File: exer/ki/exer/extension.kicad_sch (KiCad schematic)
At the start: 17 parts, among them J1 Conn_01x20, J2 Conn_01x20, J3 Conn_01x34, J4 Conn_01x34, U10 74HCT574, U11 74HCT574, U12 74LS125, U13 74LS125, U14 74HCT574

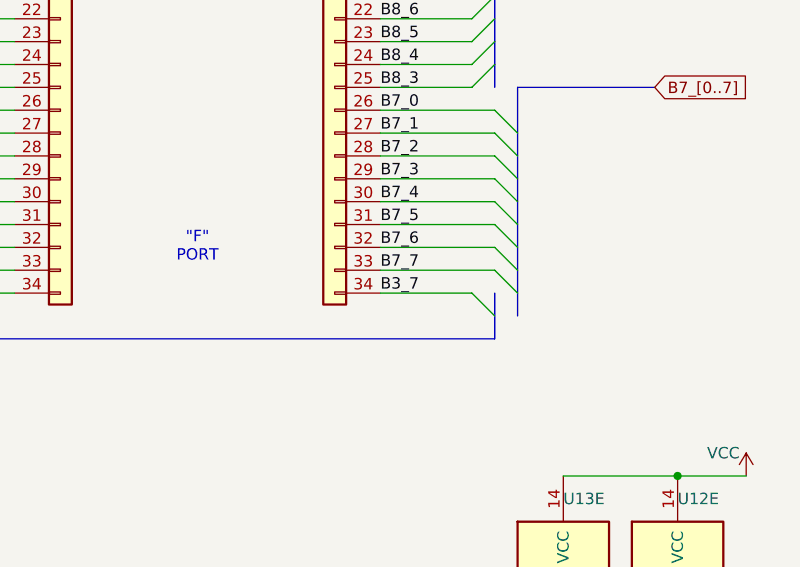
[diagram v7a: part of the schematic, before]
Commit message: Factor out functions for the t, s, and g commands to the Nano and fix a wiring error in KiCad.
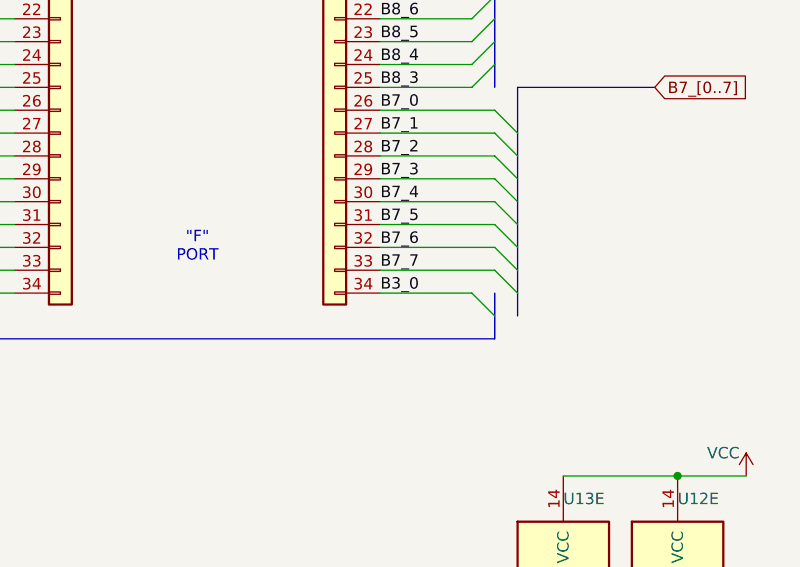
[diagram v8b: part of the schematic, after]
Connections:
- net B3_0: now also J4.34 (Pin_34)
- net B3_7: no longer J4.34 (Pin_34)
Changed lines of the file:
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@@
 		)
 	)
-	(label "B3_7"
+	(label "B3_0"
 		(at 223.52 119.38 0)
 		(fields_autoplaced yes)
@@
 	(label "B10_2"
 		(at 88.9 157.48 90)
+		(fields_autoplaced yes)
 		(effects
 			(font
@@
 	(label "B10_1"
 		(at 91.44 157.48 90)
+		(fields_autoplaced yes)
 		(effects
 			(font
@@
 	(label "B10_3"
 		(at 86.36 157.48 90)
+		(fields_autoplaced yes)
 		(effects
 			(font
@@
 	(label "B10_0"
 		(at 93.98 157.48 90)
-		(effects
-			(font
+		(fields_autoplaced yes)
+		(effects
+			(font
